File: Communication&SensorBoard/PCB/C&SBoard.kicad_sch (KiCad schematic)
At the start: 1 part, among them U1 ESP32-S3-MINI-1U

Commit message: Start the S&CBoard
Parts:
- added C1: C_Small, symbol Device:C_Small
- added J1: Conn_01x03, symbol Connector_Generic:Conn_01x03
- added J2: Micro_SD_Card, Connector_Card:microSD_HC_Molex_47219-2001, symbol Connector:Micro_SD_Card
- added R1: R_Small, symbol Device:R_Small
- added SW1: SW_Push, CompVuelo:SW_Push, symbol CompVuelo:SW_Push
- added SW2: SW_SPDT, CompVuelo:SWSPDT, symbol CompVuelo:SW_SPDT
- added U2: HDC1080, Package_SON:Texas_PWSON-N6, symbol Sensor_Humidity:HDC1080
- added U3: BMP390, CompVuelo:XDCR_BMP390L, symbol CompVuelo:BMP390
- added U4: BMI270, CompVuelo:XDCR_BMI270, symbol CompVuelo:BMI270
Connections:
- new net ESP32_{BOOT}: SW2.2
- new net ESP32_{EN}: C1.1, R1.2, SW1.2
- new net GND: C1.2, J1.3 (Pin_3), SW1.1, SW2.1
- new net UART0_{RX}: J1.1 (Pin_1)
- new net UART0_{TX}: J1.2 (Pin_2)
- new net VDD: R1.1, SW2.3

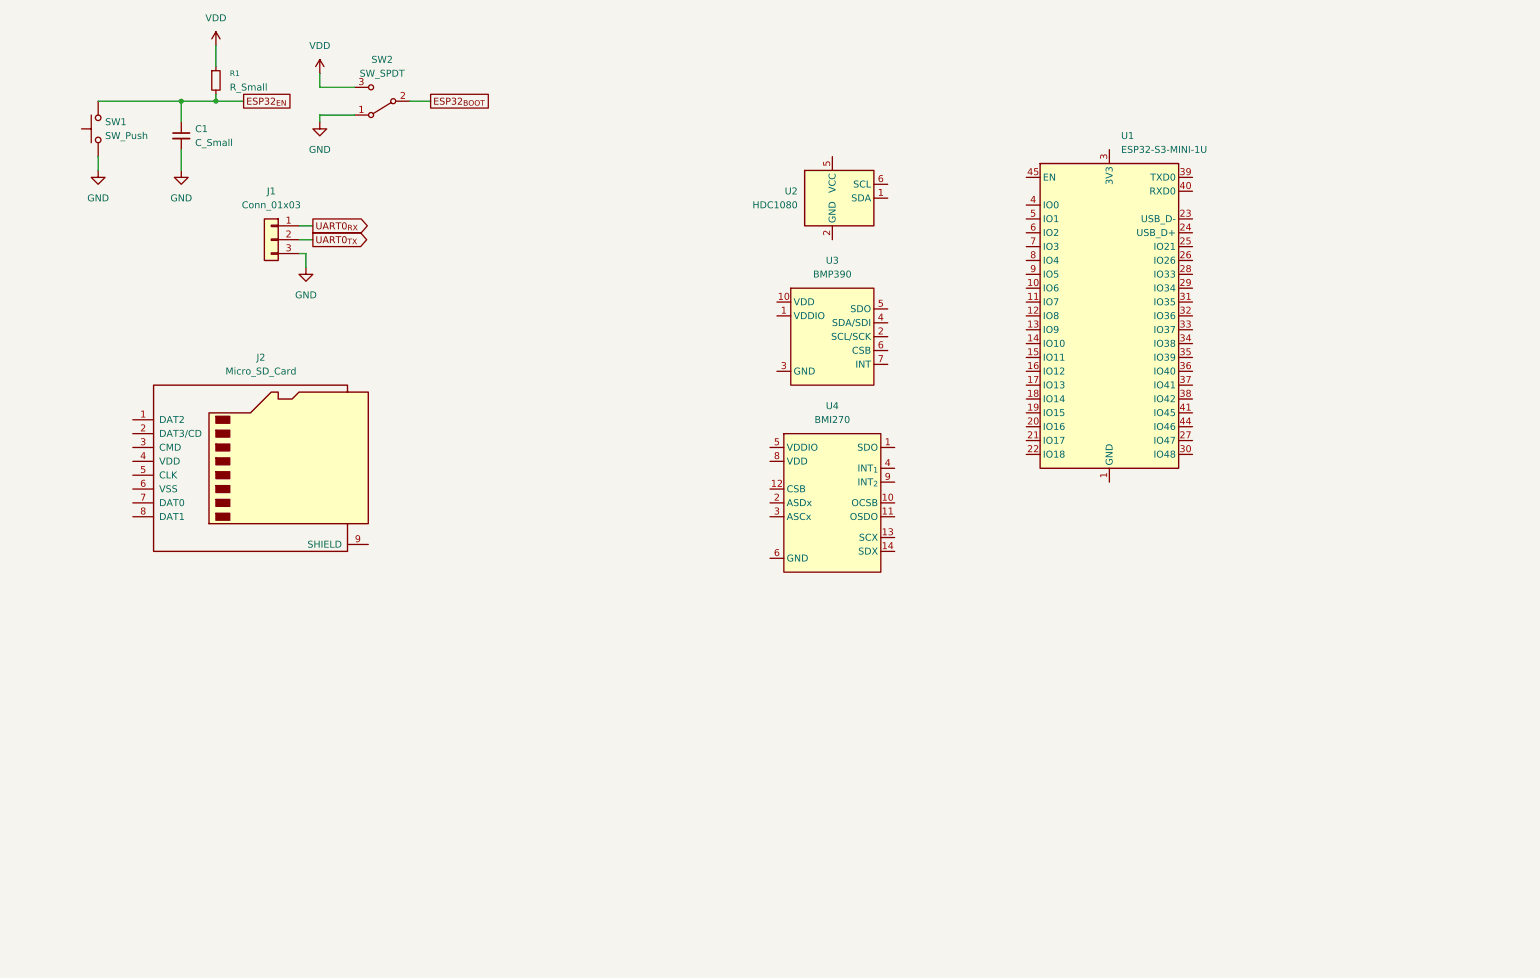
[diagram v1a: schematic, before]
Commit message: Supply & Coms-Sensor Board
la organizacion de los componentes presentes en las placas, se quedaran de esa manera, se espera que en la serigrafia se incluyan los logos de los patrocinadores, ademas se incluyo la carpeta 3D la cual contiene modelos en 3D de las dos placas, con serigrafia y componentes incluidos y ya
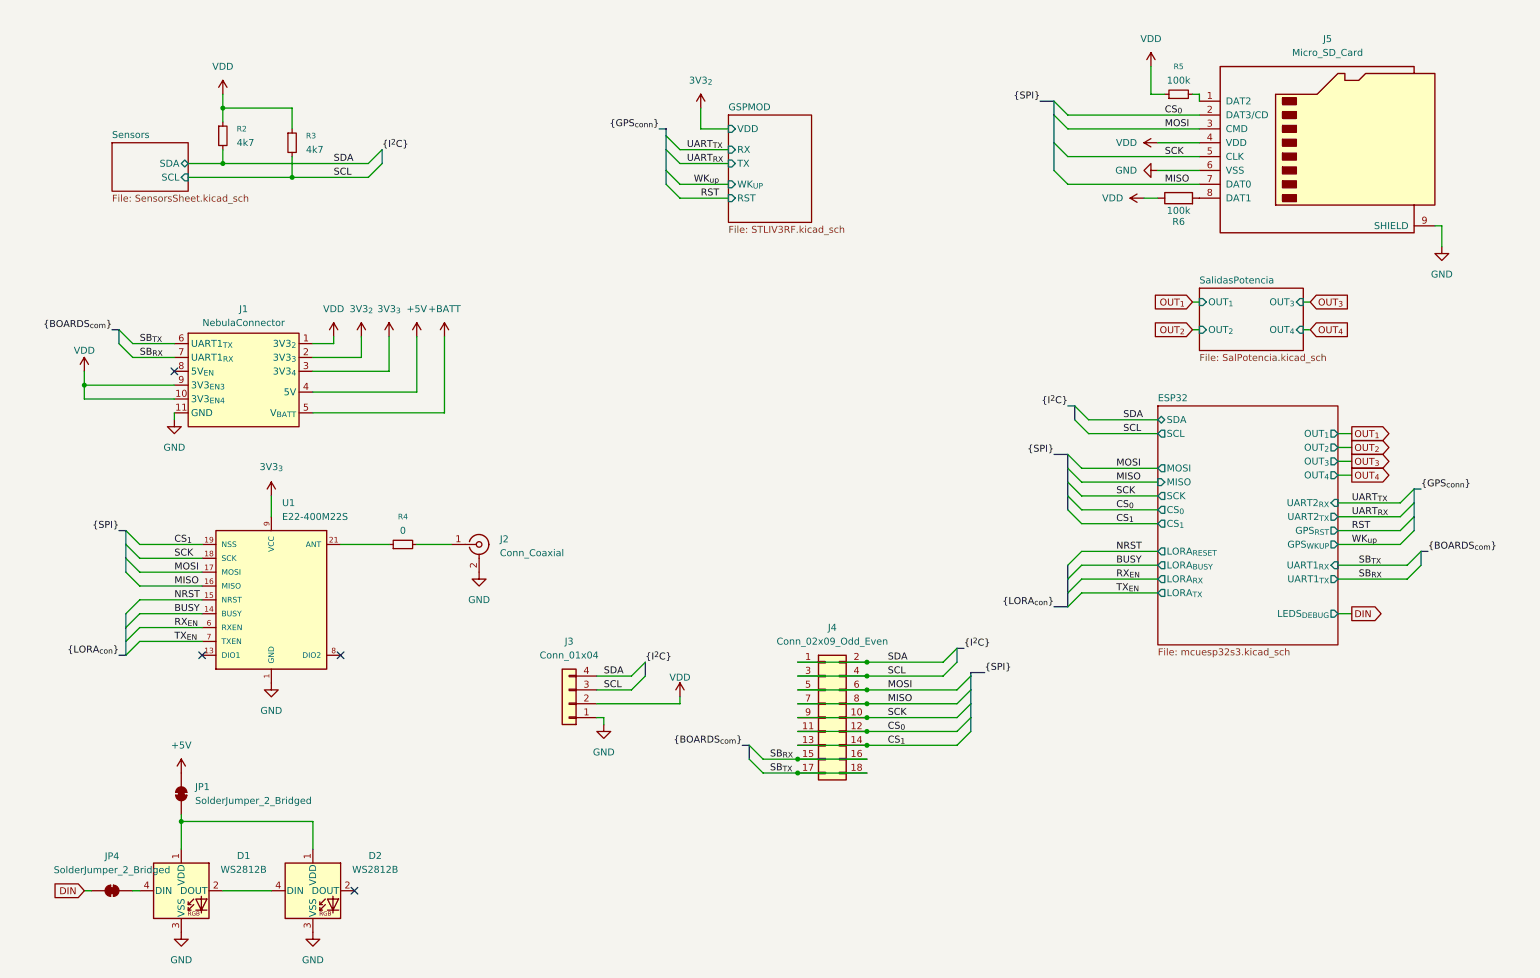
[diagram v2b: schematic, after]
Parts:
- removed C1: C_Small, symbol Device:C_Small
- removed J1: Conn_01x03, symbol Connector_Generic:Conn_01x03
- removed R1: R_Small, symbol Device:R_Small
- removed SW1: SW_Push, CompVuelo:SW_Push, symbol CompVuelo:SW_Push
- removed SW2: SW_SPDT, CompVuelo:SWSPDT, symbol CompVuelo:SW_SPDT
- removed U1: ESP32-S3-MINI-1U, RF_Module:ESP32-S2-MINI-1U, symbol RF_Module:ESP32-S3-MINI-1U
- removed U2: HDC1080, Package_SON:Texas_PWSON-N6, symbol Sensor_Humidity:HDC1080
- removed U3: BMP390, CompVuelo:XDCR_BMP390L, symbol CompVuelo:BMP390
- removed U4: BMI270, CompVuelo:XDCR_BMI270, symbol CompVuelo:BMI270
- added D1, D2: WS2812B, LED_SMD:LED_WS2812B_PLCC4_5.0x5.0mm_P3.2mm, symbol LED:WS2812B
- added J1: NebulaConnector, CompVuelo:GeneralConn, symbol CompVuelo:GeneralConn
- added J2: Conn_Coaxial, Connector_Coaxial:SMA_Molex_73251-2120_EdgeMount_Horizontal, symbol Connector:Conn_Coaxial
- added J3: Conn_01x04, Connector_PinHeader_2.54mm:PinHeader_1x04_P2.54mm_Vertical, symbol Connector_Generic:Conn_01x04
- added J4: Conn_02x09_Odd_Even, Connector_PinHeader_2.54mm:PinHeader_2x09_P2.54mm_Vertical, symbol Connector_Generic:Conn_02x09_Odd_Even
- added JP1, JP4: SolderJumper_2_Bridged, Jumper:SolderJumper-2_P1.3mm_Bridged2Bar_RoundedPad1.0x1.5mm, symbol Jumper:SolderJumper_2_Bridged
- added R2, R3: 4k7, Resistor_SMD:R_0805_2012Metric_Pad1.20x1.40mm_HandSolder, symbol Device:R_Small
- added R4: 0, Resistor_SMD:R_0805_2012Metric_Pad1.20x1.40mm_HandSolder, symbol Device:R_Small
- added R5: 100k, Resistor_SMD:R_0805_2012Metric_Pad1.20x1.40mm_HandSolder, symbol Device:R_Small
- added R6: 100k, Resistor_SMD:R_0805_2012Metric_Pad1.20x1.40mm_HandSolder, symbol Device:R
- added U1: E22-400M22S, CompVuelo:E22-400M22S, symbol CompVuelo:E22-400M22S
- renumbered J2 to J5
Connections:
- net GND: now also J5.6 (VSS), J5.9 (SHIELD), D1.3 (VSS), D2.3 (VSS), J1.11 (GND), J2.2 (Ext), J3.1 (Pin_1), U1.1 (GND)
- net VDD: now also J5.4 (VDD), J1.1 (3V3_{2}), J1.10 (3V3_{EN4}), J1.9 (3V3_{EN3}), J3.2 (Pin_2), R2.1, R3.1, R5.1, R6.1
- net at J5.1 (DAT2): now also R5.2
- net CS_{0}: now reaches J5.2 (DAT3/CD)
- net CS_{0}: now also J4.11 (Pin_11), J4.12 (Pin_12)
- net MOSI: now reaches J5.3 (CMD)
- net MOSI: now also J4.5 (Pin_5), J4.6 (Pin_6), U1.17 (MOSI)
- net SCK: now reaches J5.5 (CLK)
- net SCK: now also J4.10 (Pin_10), J4.9 (Pin_9), U1.18 (SCK)
- net MISO: now reaches J5.7 (DAT0)
- net MISO: now also J4.7 (Pin_7), J4.8 (Pin_8), U1.16 (MISO)
- net at J5.8 (DAT1): now also R6.2
- new net: D1.1 (VDD), D2.1 (VDD), JP1.1 (A)
- new net: R4.1, U1.21 (ANT)
- new net: D1.2 (DOUT), D2.4 (DIN)
- new net: D1.4 (DIN), JP4.1 (A)
- new net: J2.1 (In), R4.2
- new net +5V: J1.4 (5V), JP1.2 (B)
- new net +BATT: J1.5 (V_{BATT})
- new net 3V3_{2}: J1.2 (3V3_{3})
- new net 3V3_{3}: J1.3 (3V3_{4}), U1.9 (VCC)
- new net BUSY: U1.14 (BUSY)
- new net CS_{1}: J4.13 (Pin_13), J4.14 (Pin_14), U1.19 (NSS)
- new net DIN: JP4.2 (B)
- new net NRST: U1.15 (NRST)
- new net RX_{EN}: U1.6 (RXEN)
- new net SB_{RX}: J1.7 (UART1_{RX}), J4.15 (Pin_15), J4.16 (Pin_16)
- new net SB_{TX}: J1.6 (UART1_{TX}), J4.17 (Pin_17), J4.18 (Pin_18)
- new net SCL: J3.3 (Pin_3), J4.3 (Pin_3), J4.4 (Pin_4), R3.2
- new net SDA: J3.4 (Pin_4), J4.1 (Pin_1), J4.2 (Pin_2), R2.2
- new net TX_{EN}: U1.7 (TXEN)
- no-connect marks 0 -> 4
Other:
- added sheet ESP32 (mcuesp32s3.kicad_sch)
- added sheet GSPMOD (STLIV3RF.kicad_sch)
- added sheet SalidasPotencia (SalPotencia.kicad_sch)
- added sheet Sensors (SensorsSheet.kicad_sch)
- moved on the sheet: J5

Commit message: C&S board - update GPS
se cambio el conector del gps pasando de un sistema incorporado en placa a un sistema externo, con el BZ251
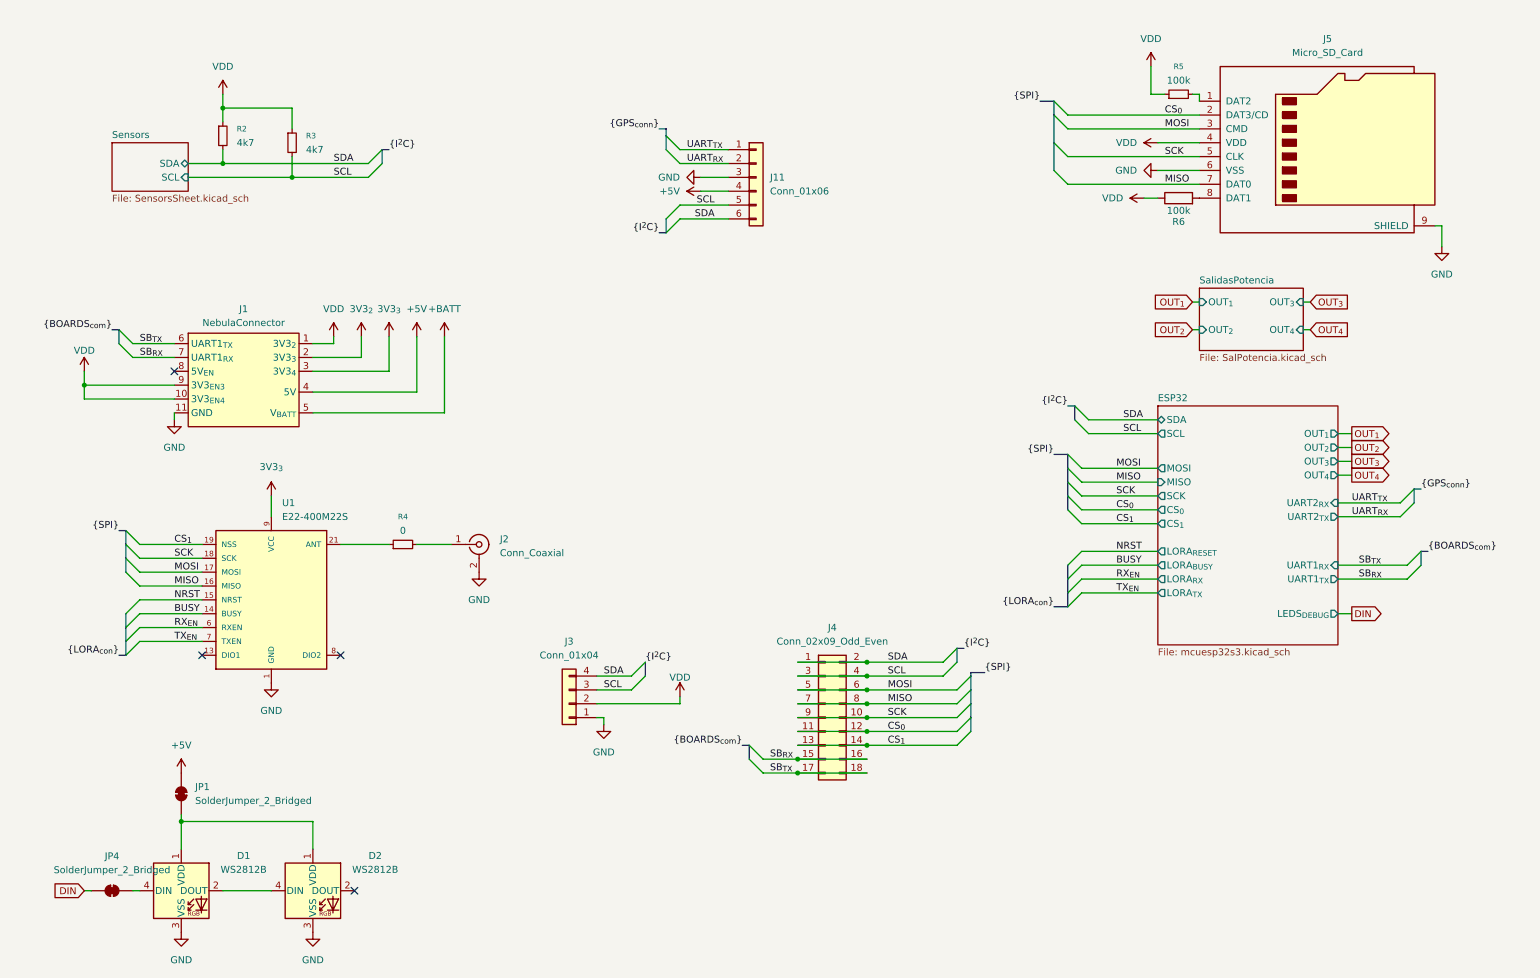
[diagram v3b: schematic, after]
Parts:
- added J11: Conn_01x06, Connector_JST:JST_SH_BM06B-SRSS-TB_1x06-1MP_P1.00mm_Vertical, symbol Connector_Generic:Conn_01x06
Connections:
- net +5V: now also J11.4 (Pin_4)
- net GND: now also J11.3 (Pin_3)
- net SCL: now also J11.5 (Pin_5)
- net SDA: now also J11.6 (Pin_6)
- net UART_{RX}: now also J11.2 (Pin_2)
- net UART_{TX}: now also J11.1 (Pin_1)
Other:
- removed sheet GSPMOD
- sheet ESP32 ports: added none; removed GPS_{RST}, GPS_{WKUP}
